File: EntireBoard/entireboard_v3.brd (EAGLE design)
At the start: 60 x 60 mm, 52 parts, among them J1 FTSH-105-01-XXX-DV-K, P1 0532610271, U1 YKA, U2 RHD2216_QFN

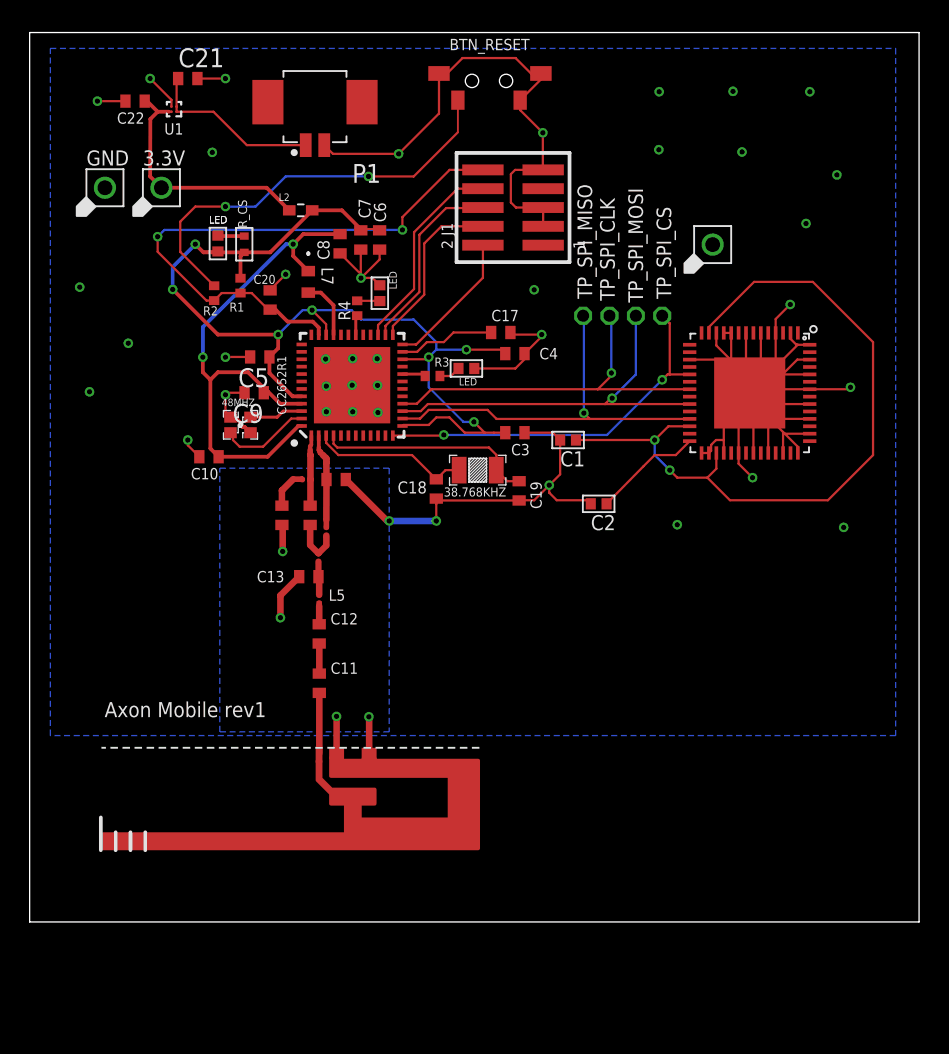
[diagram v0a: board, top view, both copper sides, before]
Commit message: modify schematics, changed parts
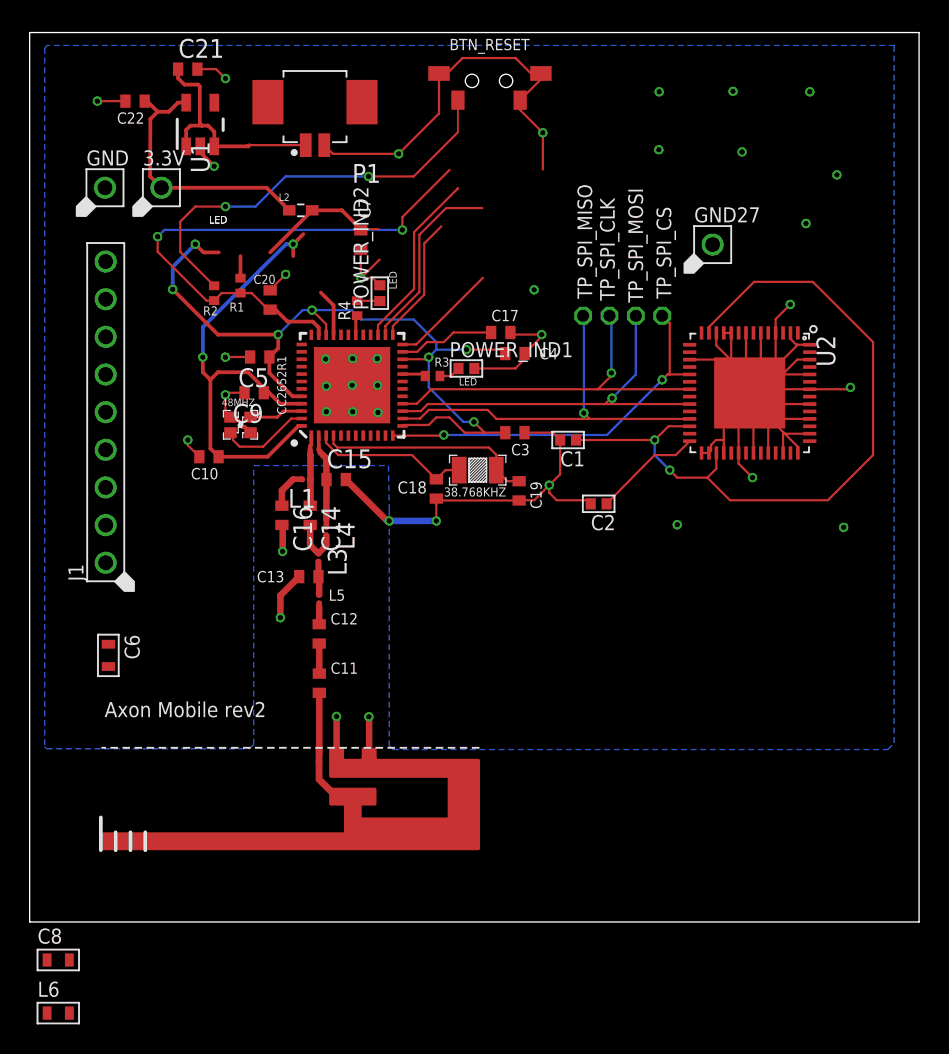
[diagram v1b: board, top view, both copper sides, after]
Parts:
- removed L7: AIML-0603-6R8K-T, inductor_0603:AIML-0603
- removed POWER_IND: LED-SMD, AxonMobile:RHD2000_EVAL_BOARD_0402
- removed R_CS: 0.01ohm, MF_Passives:R0402
- added L6: 6.8uH, MF_Passives:L0603
- C6, C8: device adafruit:C0402 -> MF_Passives:C0603
- J1: value FTSH-105-01-XXX-DV-K -> MF-CON-2.54mm-01x09; device AxonMobile:FTSH-105-01-XXX-DV-K -> MF_Connectors:PTH_2.54MM_01X09
- U1: value YKA -> TPS7A0508PDBVRDBV0005A_M; device yka0004:YKA0004ACAC -> yka0004:DBV0005A_M
- moved C8 51.9 mm to (1.93, -2.57), turned to 0 degrees
- moved C6 33.5 mm to (5.31, 18.0)
- moved J1 30.8 mm to (5.13, 34.4)
- moved U1 2.05 mm to (11.5, 53.8), turned to 90 degrees
- moved C21 0.63 mm to (10.7, 57.5)
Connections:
- removed net N$13: POWER_IND.1, R_CS.P$2
- removed net VDDS: C3.1, C4.1, C5.1, C6.1, C7.1, CC2652R1.13, CC2652R1.22, CC2652R1.34, CC2652R1.44, L2.2, POWER_IND.2, R1.2, R_CS.P$1
- new net NC: U1.4
- new net RXD: J1.P$3
- new net TXD: J1.P$4
- new net VDDS3V3: C3.1, C4.1, C5.1, C6.P$1, C7.1, CC2652R1.13, CC2652R1.22, CC2652R1.34, CC2652R1.44, J1.P$2, L2.2, R1.2
- net DCDC_SW: now also L6.P$1; no longer L7.2
- net GND: now also C6.P$2, C8.P$2, J1.P$1, U1.2; no longer C6.2, C8.2, J1.3, J1.5, J1.9, U1.B2
- net JTAG_TCK: now also J1.P$7; no longer J1.4
- net JTAG_TDI: now also J1.P$9; no longer J1.8
- net JTAG_TDO: now also J1.P$8; no longer J1.6
- net JTAG_TMS: now also J1.P$6; no longer J1.2
- net N$14: now also U1.1, U1.3; no longer U1.A1, U1.B1
- net VDDR: now also C8.P$1, L6.P$2; no longer C8.1, L7.1
- net WMCU_RESET: now also J1.P$5; no longer J1.10
- net WMCU_VDD: now also U1.5; no longer U1.A2
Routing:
- net VDDS: track 72.7 -> 0.00 mm, vias 7 -> 0
- net VDDS3V3: track 0.00 -> 67.6 mm, vias 0 -> 7
- net GND: track 175.5 -> 164.6 mm
- net VDDR: track 38.6 -> 34.7 mm
- net N$14: track 11.9 -> 15.8 mm
- net JTAG_TCK: track 11.5 -> 8.67 mm
- net WMCU_RESET: track 39.2 -> 37.0 mm
- net JTAG_TMS: track 9.51 -> 7.31 mm
- net N$13: track 1.79 -> 0.00 mm
- net JTAG_TDI: track 13.8 -> 12.1 mm
- net WMCU_VDD: track 17.0 -> 18.2 mm
- net DCDC_SW: track 4.05 -> 3.20 mm
- removed copper zone on layer 15, net N$28
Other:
- board text added: "Axon Mobile rev2"
- board text removed: "Axon Mobile rev1"
